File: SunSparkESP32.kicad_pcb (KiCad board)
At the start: 4 copper layers, 40.6 x 59.7 mm, 46 parts, among them J1 Conn_01x02_Pin, J2 USB_C_Receptacle_USB2.0, J3 Conn_01x03_Pin, J4 Conn_01x15_Pin, J5 Conn_01x03_Pin, J6 Conn_01x15_Pin, Q1 IRLML6244TRPBF, SW1 SW_Push, SW2 SW_Push, U1 ADP5090ACP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

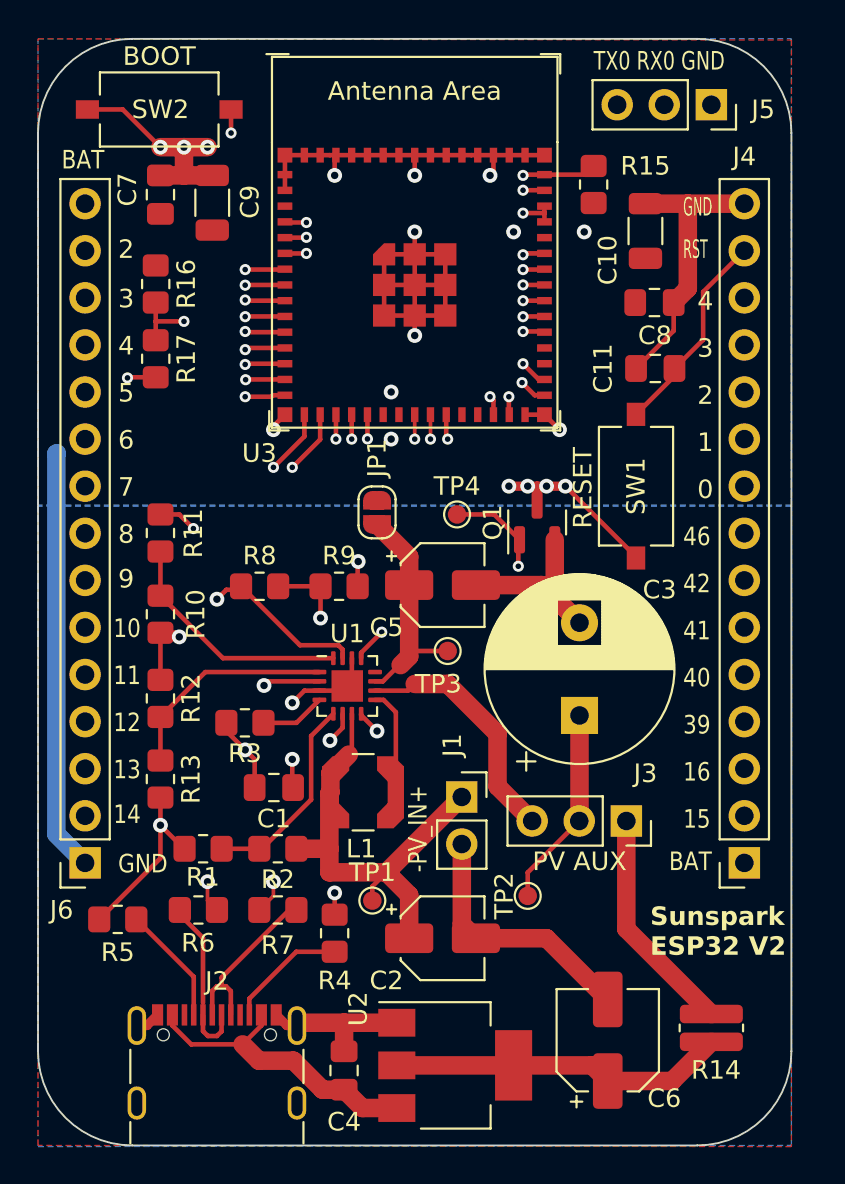
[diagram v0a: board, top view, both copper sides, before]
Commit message: Reworked placement of components Added low side switch instead of complicated high side IC Enhanced readme
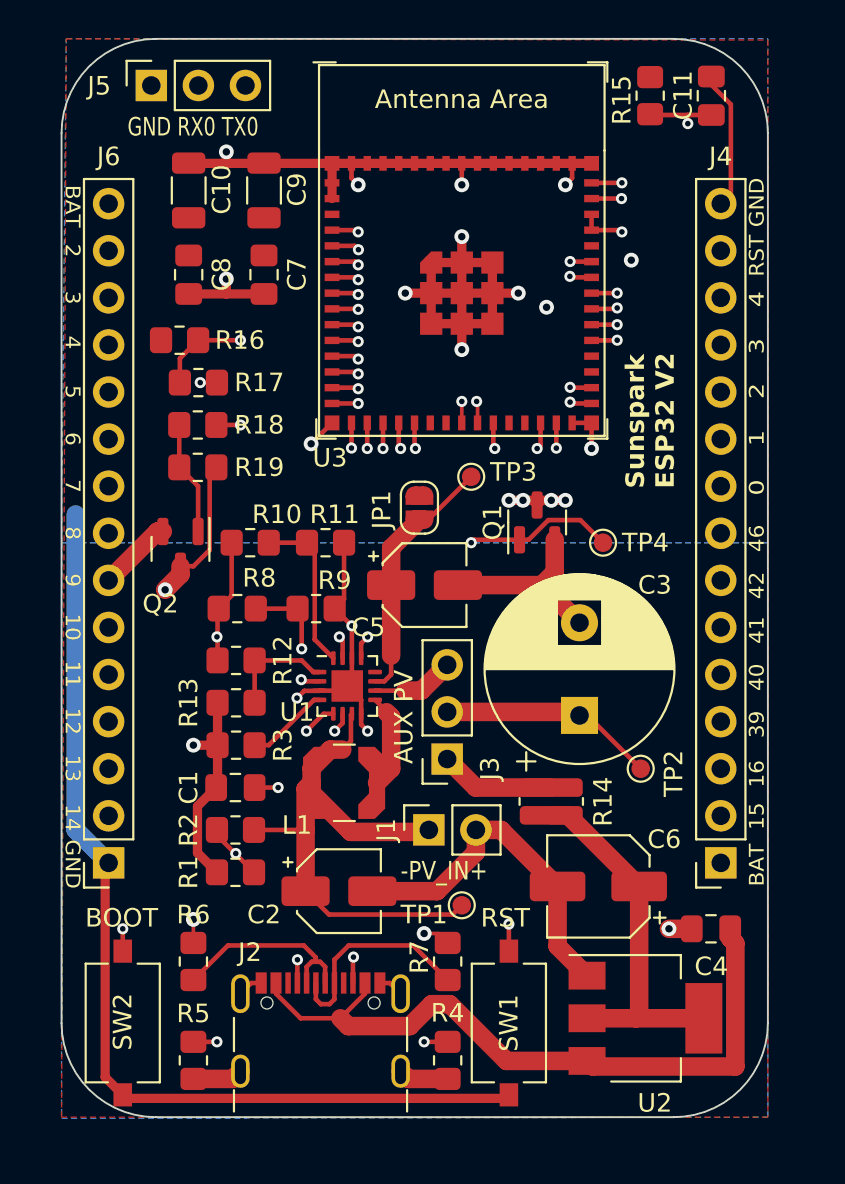
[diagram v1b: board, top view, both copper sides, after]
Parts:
- added Q2: IRLML6244TRPBF, Package_TO_SOT_SMD:SOT-23, F.Cu at (58.5, 66.9)
- added R18: 20k, Resistor_SMD:R_0805_2012Metric_Pad1.20x1.40mm_HandSolder, F.Cu at (59.4, 60.2)
- added R19: 20k, Resistor_SMD:R_0805_2012Metric_Pad1.20x1.40mm_HandSolder, F.Cu at (59.4, 62.5)
- moved SW2 49.3 mm to (55.4, 92.5), turned to 90 degrees
- moved J5 30.2 mm to (56.9, 41.9), turned to 90 degrees
- moved SW1 29.8 mm to (76.2, 92.5)
- moved C8 25.2 mm to (58.9, 52.1), turned to -90 degrees
- moved C10 24.7 mm to (58.9, 47.5)
- moved C4 21.2 mm to (87.1, 87.4), turned to 180 degrees
- moved C11 15.0 mm to (87.1, 42.4), turned to 90 degrees
- moved R14 15.0 mm to (78.5, 80.5)
- moved U2 10.6 mm to (83.6, 92.2)
- moved J3 10.2 mm to (72.9, 78.2), turned to 180 degrees
- moved R7 9.57 mm to (72.9, 89.1), turned to 90 degrees
- moved TP3 9.48 mm to (74.2, 63.0)
- moved TP2 9.18 mm to (83.3, 78.7)
- moved R4 9.18 mm to (72.9, 94.5), turned to 90 degrees
- moved R11 8.92 mm to (66.3, 66.5), turned to 0 degrees
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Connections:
- J6 pad 7: Net-(J6-Pin_7) -> AUX_SW
- U3 pad 13: Net-(J6-Pin_7) -> AUX_SW_CTRL
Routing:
- net boot_btn: track 8.95 -> 46.6 mm
- net rst_btn: track 28.9 -> 62.9 mm, vias 1 -> 3
- net GND1: track 107.5 -> 130.0 mm, vias 16 -> 17
- net VBUS: track 16.5 -> 38.0 mm
- net Net-(J6-Pin_7): track 17.4 -> 0.00 mm, vias 1 -> 0
- net GND: track 59.8 -> 72.1 mm, vias 7 -> 6
- net Net-(J5-Pin_2): track 14.4 -> 25.1 mm
- net AUX_SW_CTRL: track 0.00 -> 10.2 mm, vias 0 -> 2
- net Net-(J3-Pin_3): track 13.3 -> 4.47 mm
- net USB_DP: track 30.5 -> 38.3 mm
- net Net-(Q2-G): track 0.00 -> 6.17 mm
- net V_AUX: track 12.3 -> 6.25 mm
- net Net-(U1-SETSD): track 11.9 -> 6.04 mm
- net USB_DN: track 31.7 -> 36.9 mm
- net Net-(J1-Pin_1): track 25.6 -> 30.7 mm
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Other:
- board size 40.6 x 59.7 mm -> 38.1 x 58.2 mm
- board text added: "AUX PV"
- board text added: "GND RX0 TX0"
- board text removed: "PV AUX"
- board text removed: "RESET"
- board text removed: "TX0 RX0 GND"
- board text removed: "{ "ViaStitching": "0.2", "stitch_zone_0": { "HSpacing": "0.1", "VSpacing": "0.1", "Clearance": "0", "Randomize": false } }"

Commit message: Minor enhancements to PCB Added BOM and PDF output
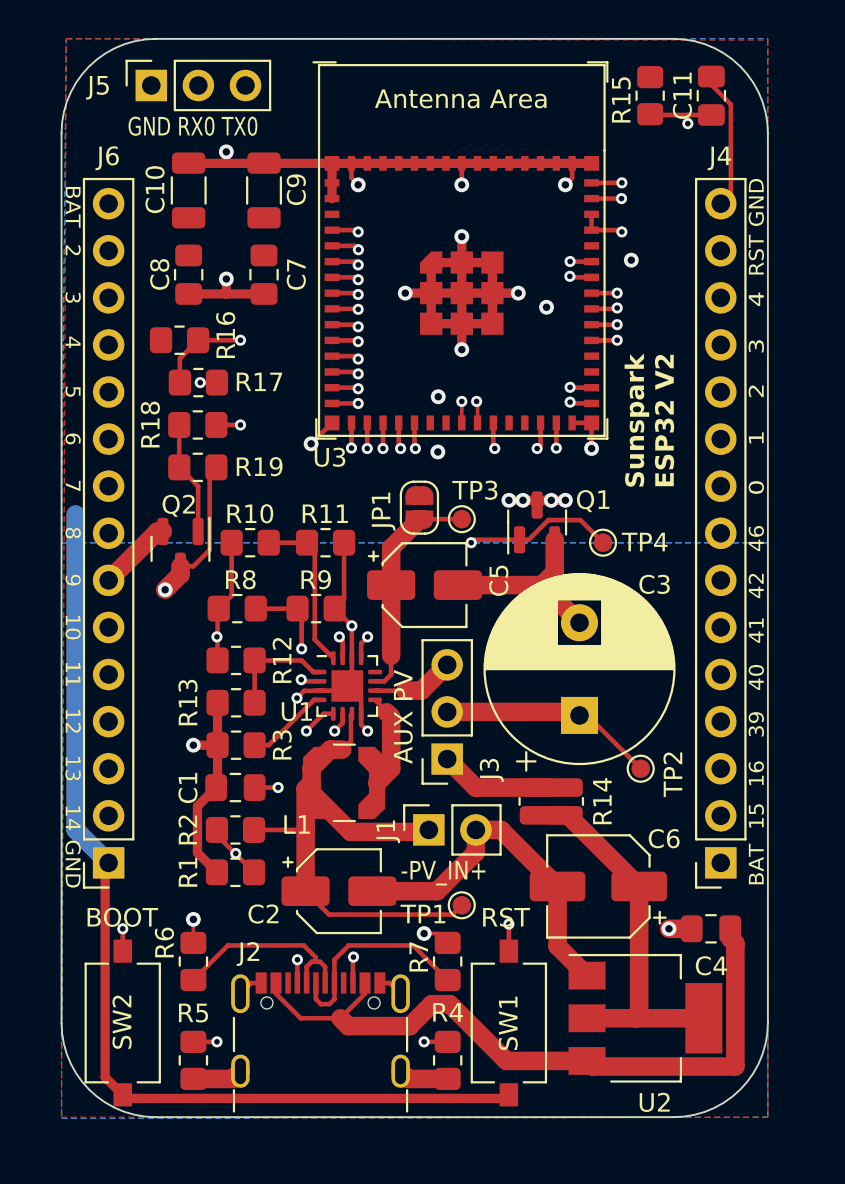
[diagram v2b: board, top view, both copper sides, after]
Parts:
- moved TP3 2.34 mm to (73.7, 65.3)
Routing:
- net USB_DP: track 38.3 -> 33.3 mm
- net +BATT: track 5.62 -> 8.61 mm, vias 2 -> 4
- net USB_DN: track 36.9 -> 39.7 mm
- net Net-(JP1-A): track 13.8 -> 12.3 mm
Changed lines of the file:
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@@
     (property "ki_keywords" "R res resistor")
     (attr smd)
-    (fp_text reference "R18" (at -3.318 0) (layer "F.SilkS")
+    (fp_text reference "R18" (at 2.524 0 90) (layer "F.SilkS")
         (effects (font (size 1 1) (thickness 0.15)))
     )
@@
     (property "ki_keywords" "R res resistor")
     (attr smd)
-    (fp_text reference "R6" (at 2.524 0 180) (layer "F.SilkS")
+    (fp_text reference "R6" (at 1 -1.524 270) (layer "F.SilkS")
         (effects (font (size 1 1) (thickness 0.15)))
     )
@@
   )
   (footprint "TestPoint:TestPoint_Pad_D1.0mm" (layer "F.Cu")
-    (at 74.168 62.992)
+    (at 73.66 65.278)
     (descr "SMD pad as test Point, diameter 1.0mm")
     (tags "test point SMD pad")
@@
     (property "ki_keywords" "test point tp")
     (attr exclude_from_pos_files)
-    (fp_text reference "TP3" (at 2.286 -0.254 180) (layer "F.SilkS")
+    (fp_text reference "TP3" (at 0.762 -1.524 180) (layer "F.SilkS")
         (effects (font (size 1 1) (thickness 0.15)))
     )
@@
     (property "ki_keywords" "R res resistor")
     (attr smd)
-    (fp_text reference "R9" (at 1 -1.524) (layer "F.SilkS")
+    (fp_text reference "R9" (at -0.016 -1.524) (layer "F.SilkS")
         (effects (font (size 1 1) (thickness 0.15)))
     )
@@
     (property "ki_keywords" "cap capacitor")
     (attr smd)
-    (fp_text reference "C8" (at -0.0215 -1.778 90) (layer "F.SilkS")
+    (fp_text reference "C8" (at -0.0215 1.524 90) (layer "F.SilkS")
         (effects (font (size 1 1) (thickness 0.15)))
     )
@@
     (property "ki_keywords" "R res resistor")
     (attr smd)
-    (fp_text reference "R8" (at 1.19 -1.65) (layer "F.SilkS")
+    (fp_text reference "R8" (at 0.174 -1.524) (layer "F.SilkS")
         (effects (font (size 1 1) (thickness 0.15)))
     )
@@
     (property "ki_keywords" "N-Channel Switching MOSFET")
     (attr smd)
-    (fp_text reference "Q1" (at 0 -2.4 90) (layer "F.SilkS")
+    (fp_text reference "Q1" (at 1.1915 3.048 180) (layer "F.SilkS")
         (effects (font (size 1 1) (thickness 0.15)))
     )
@@
     (property "ki_keywords" "cap capacitor")
     (attr smd)
-    (fp_text reference "C5" (at -3.026 2.286) (layer "F.SilkS")
+    (fp_text reference "C5" (at 4.042 -0.254 90) (layer "F.SilkS")
         (effects (font (size 1 1) (thickness 0.15)))
     )
@@
     (property "ki_keywords" "R res resistor")
     (attr smd)
-    (fp_text reference "R11" (at 0.492 -1.524 180) (layer "F.SilkS")
+    (fp_text reference "R11" (at -0.016 -1.524 180) (layer "F.SilkS")
         (effects (font (size 1 1) (thickness 0.15)))
     )
@@
     (property "ki_keywords" "R res resistor")
     (attr smd)
-    (fp_text reference "R10" (at 1.444 -1.524 180) (layer "F.SilkS")
+    (fp_text reference "R10" (at -0.016 -1.524 180) (layer "F.SilkS")
         (effects (font (size 1 1) (thickness 0.15)))
     )
@@
     (property "ki_keywords" "cap capacitor")
     (attr smd)
-    (fp_text reference "C10" (at 0.049 1.778 90) (layer "F.SilkS")
+    (fp_text reference "C10" (at 0.049 -1.778 90) (layer "F.SilkS")
         (effects (font (size 1 1) (thickness 0.15)))
     )
@@
     (property "ki_keywords" "N-Channel Switching MOSFET")
     (attr smd)
-    (fp_text reference "Q2" (at 2.9695 1.082 -180) (layer "F.SilkS")
+    (fp_text reference "Q2" (at -2.3645 0.066 -180) (layer "F.SilkS")
         (effects (font (size 1 1) (thickness 0.15)))
     )
@@
     (property "ki_keywords" "R res resistor")
     (attr smd)
-    (fp_text reference "R16" (at 3.254 0 180) (layer "F.SilkS")
+    (fp_text reference "R16" (at 2.524 -0.254 -90) (layer "F.SilkS")
         (effects (font (size 1 1) (thickness 0.15)))
     )
@@
   (segment (start 78.486 79.756) (end 74.412 79.756) (width 1) (layer "F.Cu") (net 5))
   (segment (start 74.412 79.756) (end 72.873 78.217) (width 1) (layer "F.Cu") (net 5))
+  (via (at 72.39 58.674) (size 0.8) (drill 0.4) (layers "F.Cu" "B.Cu") (free) (net 6))
   (via (at 82.804 51.308) (size 0.8) (drill 0.4) (layers "F.Cu" "B.Cu") (free) (net 6))
+  (via (at 72.3685 61.654399) (size 0.8) (drill 0.4) (layers "F.Cu" "B.Cu") (free) (net 6))
   (via (at 78.232 53.848) (size 0.8) (drill 0.4) (layers "F.Cu" "B.Cu") (free) (net 6))
+  (segment (start 72.3685 58.6955) (end 72.39 58.674) (width 0.5) (layer "In1.Cu") (net 6))
+  (segment (start 72.3685 61.654399) (end 72.3685 58.6955) (width 0.5) (layer "In1.Cu") (net 6))
   (segment (start 81.788 51.308) (end 82.804 51.308) (width 0.5) (layer "In2.Cu") (net 6))
   (segment (start 78.232 53.848) (end 79.248 53.848) (width 0.5) (layer "In2.Cu") (net 6))
@@
   (via (at 59.182 86.868) (size 0.8) (drill 0.4) (layers "F.Cu" "B.Cu") (net 43))
   (via (at 73.66 58.928) (size 0.6) (drill 0.3) (layers "F.Cu" "B.Cu") (net 43))
-  (segment (start 64.798999 81.251001) (end 59.182 86.868) (width 0.2) (layer "In2.Cu") (net 43))
-  (segment (start 64.798999 77.077528) (end 64.798999 81.251001) (width 0.2) (layer "In2.Cu") (net 43))
-  (segment (start 73.66 58.928) (end 73.66 60.452) (width 0.2) (layer "In2.Cu") (net 43))
-  (segment (start 64.17 76.448529) (end 64.798999 77.077528) (width 0.2) (layer "In2.Cu") (net 43))
-  (segment (start 64.798999 69.313001) (end 64.798999 71.649972) (width 0.2) (layer "In2.Cu") (net 43))
-  (segment (start 73.66 60.452) (end 64.798999 69.313001) (width 0.2) (layer "In2.Cu") (net 43))
-  (segment (start 64.798999 71.649972) (end 64.17 72.278971) (width 0.2) (layer "In2.Cu") (net 43))
-  (segment (start 64.17 72.278971) (end 64.17 76.448529) (width 0.2) (layer "In2.Cu") (net 43))
+  (segment (start 64.7058 86.868) (end 59.182 86.868) (width 0.2) (layer "In2.Cu") (net 43))
+  (segment (start 73.834751 59.102751) (end 73.834751 65.39635) (width 0.2) (layer "In2.Cu") (net 43))
+  (segment (start 73.66 58.928) (end 73.834751 59.102751) (width 0.2) (layer "In2.Cu") (net 43))
+  (segment (start 70.282019 68.949082) (end 70.282019 81.291781) (width 0.2) (layer "In2.Cu") (net 43))
+  (segment (start 73.834751 65.39635) (end 70.282019 68.949082) (width 0.2) (layer "In2.Cu") (net 43))
+  (segment (start 70.282019 81.291781) (end 64.7058 86.868) (width 0.2) (layer "In2.Cu") (net 43))
   (segment (start 74.459503 58.928) (end 74.51 58.978497) (width 0.2) (layer "F.Cu") (net 44))
   (segment (start 72.898 88.138) (end 72.39 87.63) (width 0.2) (layer "F.Cu") (net 44))
@@
   (via (at 74.459503 58.928) (size 0.6) (drill 0.3) (layers "F.Cu" "B.Cu") (net 44))
   (via (at 71.628 87.63) (size 0.8) (drill 0.4) (layers "F.Cu" "B.Cu") (net 44))
-  (segment (start 65.249001 71.649972) (end 65.878 72.278971) (width 0.2) (layer "In2.Cu") (net 44))
-  (segment (start 65.249001 81.251001) (end 71.628 87.63) (width 0.2) (layer "In2.Cu") (net 44))
-  (segment (start 65.878 76.956529) (end 65.249001 77.585528) (width 0.2) (layer "In2.Cu") (net 44))
-  (segment (start 65.249001 77.585528) (end 65.249001 81.251001) (width 0.2) (layer "In2.Cu") (net 44))
-  (segment (start 74.459503 58.928) (end 74.459503 60.414497) (width 0.2) (layer "In2.Cu") (net 44))
-  (segment (start 74.459503 60.414497) (end 65.249001 69.624999) (width 0.2) (layer "In2.Cu") (net 44))
-  (segment (start 65.249001 69.624999) (end 65.249001 71.649972) (width 0.2) (layer "In2.Cu") (net 44))
-  (segment (start 65.878 72.278971) (end 65.878 76.956529) (width 0.2) (layer "In2.Cu") (net 44))
+  (segment (start 74.284752 59.102751) (end 74.284752 65.582719) (width 0.2) (layer "In2.Cu") (net 44))
+  (segment (start 70.732 69.135471) (end 70.732 86.734) (width 0.2) (layer "In2.Cu") (net 44))
+  (segment (start 74.284752 65.582719) (end 70.732 69.135471) (width 0.2) (layer "In2.Cu") (net 44))
+  (segment (start 70.732 86.734) (end 71.628 87.63) (width 0.2) (layer "In2.Cu") (net 44))
+  (segment (start 74.459503 58.928) (end 74.284752 59.102751) (width 0.2) (layer "In2.Cu") (net 44))
   (segment (start 68.084802 50.74336) (end 67.877442 50.536) (width 0.25) (layer "F.Cu") (net 45))
   (segment (start 59.436 55.626) (end 58.452 56.61) (width 0.25) (layer "F.Cu") (net 45))
@@
   (segment (start 65.981 73.527) (end 65.653 73.527) (width 0.25) (layer "F.Cu") (net 48))
   (segment (start 69.85 72.644) (end 69.85 73.66) (width 0.25) (layer "F.Cu") (net 55))
+  (segment (start 73.66 65.278) (end 71.404 65.278) (width 0.25) (layer "F.Cu") (net 55))
   (segment (start 69.85 68.834) (end 69.85 72.644) (width 1) (layer "F.Cu") (net 55))
   (segment (start 69.483 74.027) (end 68.981 74.027) (width 0.25) (layer "F.Cu") (net 55))
   (segment (start 69.85 73.66) (end 69.483 74.027) (width 0.25) (layer "F.Cu") (net 55))
-  (segment (start 71.852 65.308) (end 71.374 65.308) (width 0.25) (layer "F.Cu") (net 55))
-  (segment (start 74.168 62.992) (end 71.852 65.308) (width 0.25) (layer "F.Cu") (net 55))
   (segment (start 69.85 66.832) (end 71.374 65.308) (width 1) (layer "F.Cu") (net 55))
+  (segment (start 71.404 65.278) (end 71.374 65.308) (width 0.25) (layer "F.Cu") (net 55))
   (segment (start 69.85 68.834) (end 69.85 66.832) (width 1) (layer "F.Cu") (net 55))
   (segment (start 64.79 89.04943) (end 64.79 90.3) (width 0.25) (layer "F.Cu") (net 56))

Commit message: Added optional footprint for RF95/96/97/98 footprint
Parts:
- added J7: Conn_01x01_Pin, TestPoint:TestPoint_THTPad_D1.5mm_Drill0.7mm, B.Cu at (62.2, 64.0)
- added U4: RFM96W-433S2, RF_Module:HOPERF_RFM9XW_SMD, B.Cu at (64.8, 54.4)
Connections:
- net Net-(J6-Pin_3) renamed MISO
- net Net-(J6-Pin_4) renamed SCLK
- net Net-(J6-Pin_5) renamed MOSI
- net Net-(J6-Pin_6) renamed CS0
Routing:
- net rst_btn: track 62.9 -> 81.0 mm, vias 3 -> 4
- net MISO: track 24.4 -> 39.7 mm, vias 1 -> 2
- net CS0: track 20.4 -> 32.1 mm, vias 1 -> 2
- net SCLK: track 21.6 -> 32.9 mm, vias 1 -> 2
- net MOSI: track 21.6 -> 32.5 mm, vias 1 -> 2
- net +BATT: track 8.61 -> 14.8 mm, vias 4 -> 6
- net Net-(J7-Pin_1): track 0.00 -> 6.08 mm
- net GND1: track 130.0 -> 124.7 mm, vias 17 -> 13
- net Net-(J4-Pin_3): track 27.0 -> 30.8 mm
- net Net-(J6-Pin_8): track 18.8 -> 16.0 mm
- net Net-(J6-Pin_9): track 18.1 -> 15.3 mm
- net USB_DP: track 33.3 -> 34.8 mm
- net USB_DN: track 39.7 -> 41.0 mm
- net /IO0: track 14.4 -> 15.0 mm
